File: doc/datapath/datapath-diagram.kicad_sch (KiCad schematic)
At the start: 22 parts, among them U17 ip, U19 insn, U27 stack[0], U28 stack[1], U29 ……, U32 cd_timer, U4 cstack[0], U5 cstack[1], U6 ……

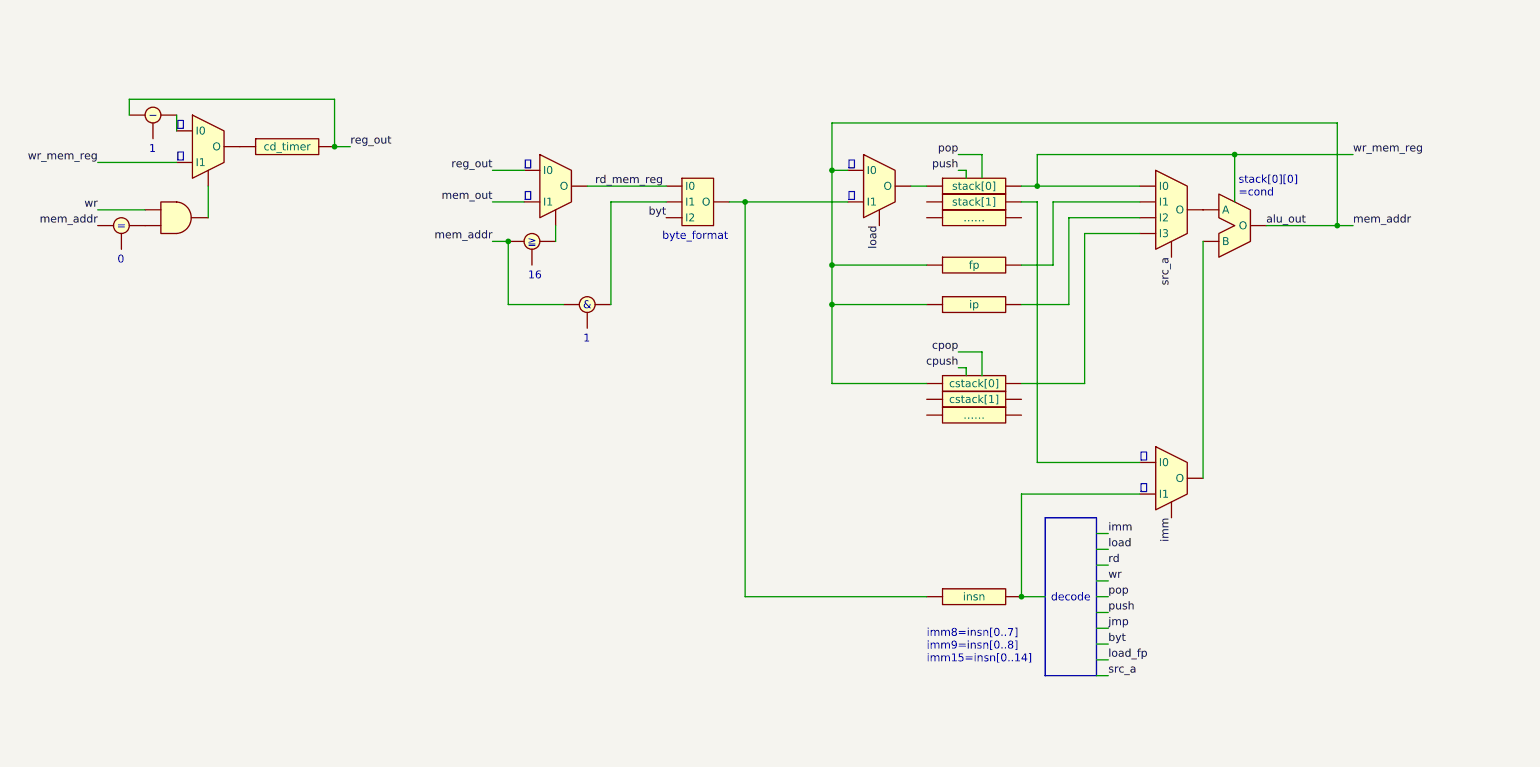
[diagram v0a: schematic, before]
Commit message: アドレスマップ（ドキュメント）を修正
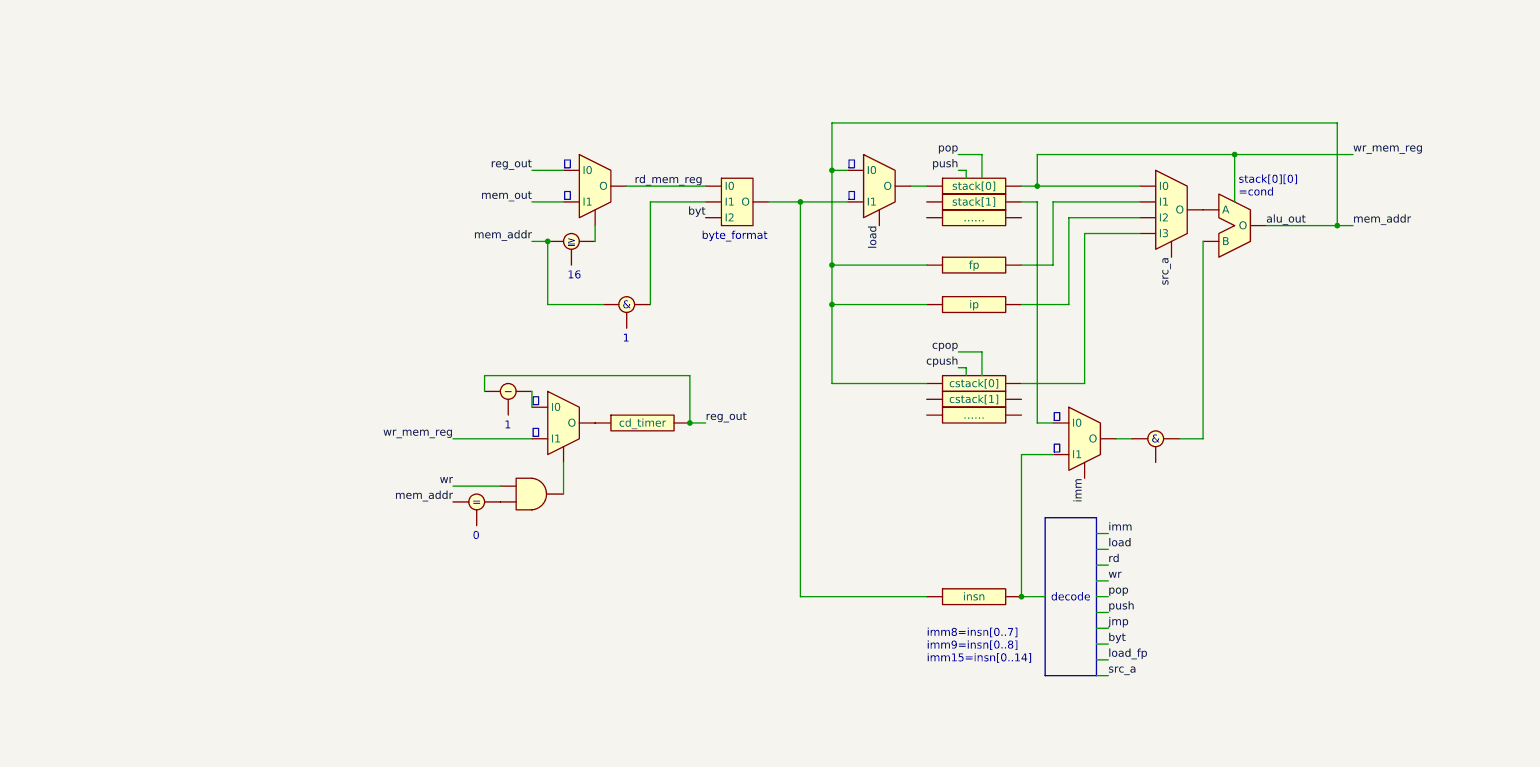
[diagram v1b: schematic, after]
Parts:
- added U2: ~, symbol Logic_Component:ALU_Circle_Left_Bottom
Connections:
- net at U28.: now also U15. (O)
- new net: U1., U31. (O)
- new net: U18. (O), U19., U34. (O)
- new net: U18. (O), U27.
- new net: U32., U36. (O)
- new net: U33., U34. (O)
- new net: U., U40. (O)
- new net: U17., U40. (O)
- new net: U4., U40. (O)
- new net: U12. (O), U40. (O)
- new net: U36. (O), U37.
- new net: U12. (O), U2.
- new net: U15. (O), U2.
- new net: U36. (O), U39.
- new net: U38., U39.

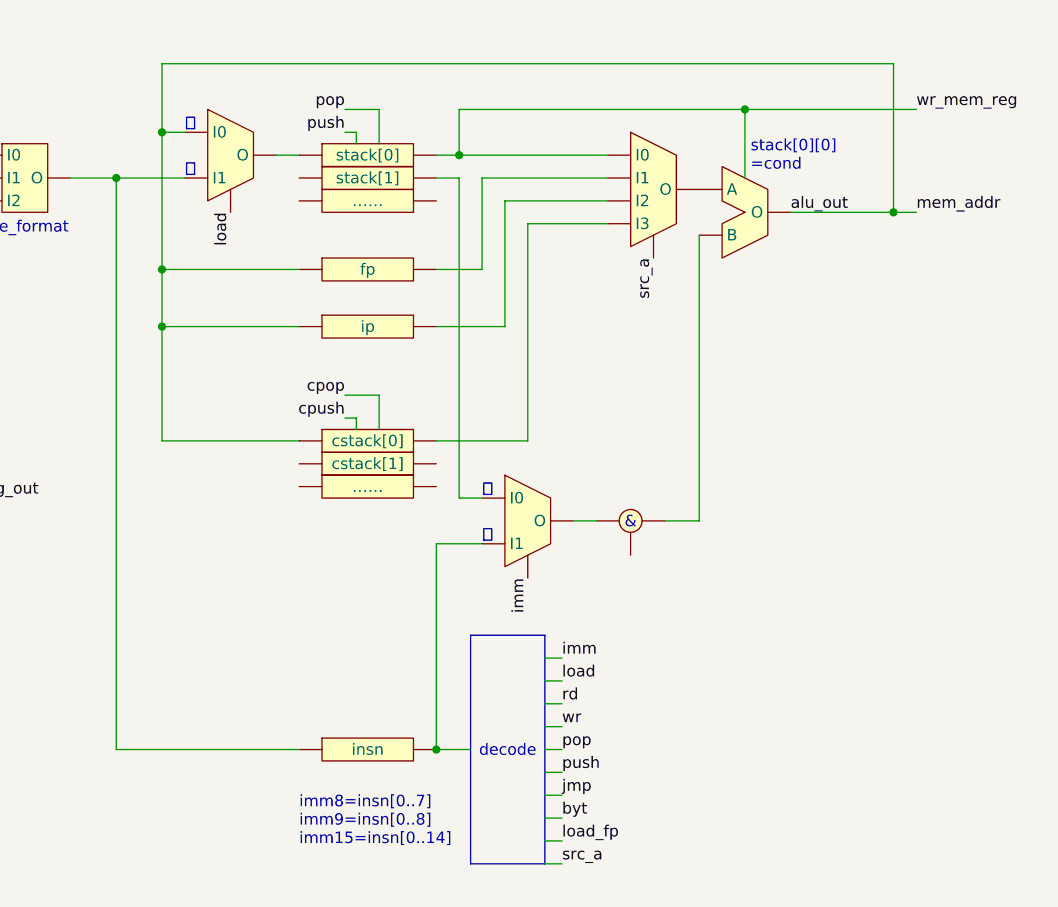
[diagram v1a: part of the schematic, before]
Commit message: データパス図を更新
メモリへ書き込むデータをstack[0]/stack[1]から選べるようにする
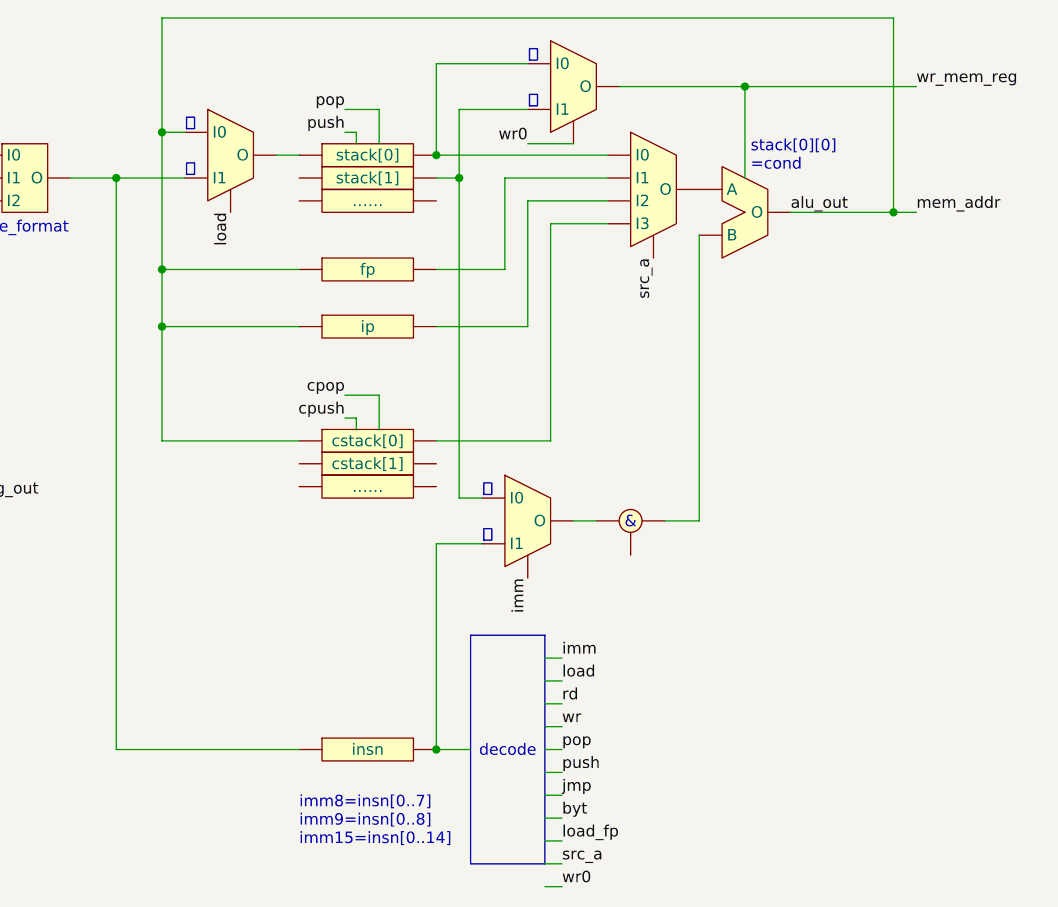
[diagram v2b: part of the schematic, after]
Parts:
- added U3: ~, symbol Logic_Component:Multiplexer_2
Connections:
- net wr_mem_reg: now also U3. (O); no longer U27., U40. (O)
- net at U28.: now also U15. (O), U3. (O)
- net at U27.: now also U40. (O), U3. (O); no longer U18. (O)
- net at U2.: now also U15. (O)
- new net: U1., U31. (O)
- new net: U18. (O), U19., U34. (O)
- new net: U18. (O), U27.
- new net: U32., U36. (O)
- new net: U33., U34. (O)
- new net: U., U40. (O)
- new net: U17., U40. (O)
- new net: U4., U40. (O)
- new net: U12. (O), U40. (O)
- new net: U36. (O), U37.
- new net: U12. (O), U2.
- new net: U36. (O), U39.
- new net: U38., U39.
- new net wr0: U3. (O)
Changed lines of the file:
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@@
   (junction (at 120.65 88.9) (diameter 0) (color 0 0 0 0)
   )
+  (junction (at 176.53 53.34) (diameter 0) (color 0 0 0 0)
+  )
+  (junction (at 173.99 50.8) (diameter 0) (color 0 0 0 0)
+  )
   (junction (at 143.51 63.5) (diameter 0) (color 0 0 0 0)
   )
@@
   (junction (at 173.99 116.84) (diameter 0) (color 0 0 0 0)
   )
+  (junction (at 208.28 43.18) (diameter 0) (color 0 0 0 0)
+  )
   (junction (at 143.51 48.26) (diameter 0) (color 0 0 0 0)
   )
-  (junction (at 208.28 45.72) (diameter 0) (color 0 0 0 0)
-  )
   (junction (at 138.43 53.34) (diameter 0) (color 0 0 0 0)
   )
-  (junction (at 176.53 50.8) (diameter 0) (color 0 0 0 0)
-  )
   (junction (at 224.79 57.15) (diameter 0) (color 0 0 0 0)
   )
+  (wire (pts (xy 186.055 132.08) (xy 187.96 132.08))
+    (stroke (width 0) (type default))
+  )
   (wire (pts (xy 167.64 77.47) (xy 167.64 81.28))
     (stroke (width 0) (type default))
@@
     (stroke (width 0) (type default))
   )
-  (wire (pts (xy 181.61 55.88) (xy 193.04 55.88))
+  (wire (pts (xy 184.15 55.88) (xy 193.04 55.88))
     (stroke (width 0) (type default))
   )
@@
     (stroke (width 0) (type default))
   )
-  (wire (pts (xy 173.99 82.55) (xy 184.15 82.55))
-    (stroke (width 0) (type default))
-  )
-  (wire (pts (xy 143.51 40.64) (xy 143.51 48.26))
+  (wire (pts (xy 173.99 82.55) (xy 186.69 82.55))
+    (stroke (width 0) (type default))
+  )
+  (wire (pts (xy 143.51 35.56) (xy 143.51 48.26))
     (stroke (width 0) (type default))
   )
@@
     (stroke (width 0) (type default))
   )
-  (wire (pts (xy 176.53 50.8) (xy 193.04 50.8))
-    (stroke (width 0) (type default))
-  )
   (wire (pts (xy 95.25 53.34) (xy 100.33 53.34))
     (stroke (width 0) (type default))
@@
     (stroke (width 0) (type default))
   )
-  (wire (pts (xy 173.99 50.8) (xy 176.53 50.8))
+  (wire (pts (xy 173.99 50.8) (xy 193.04 50.8))
     (stroke (width 0) (type default))
   )
@@
     (stroke (width 0) (type default))
   )
+  (wire (pts (xy 176.53 45.72) (xy 176.53 53.34))
+    (stroke (width 0) (type default))
+  )
   (wire (pts (xy 173.99 116.84) (xy 177.8 116.84))
     (stroke (width 0) (type default))
@@
     (stroke (width 0) (type default))
   )
+  (wire (pts (xy 184.15 49.53) (xy 189.23 49.53))
+    (stroke (width 0) (type default))
+  )
   (wire (pts (xy 186.055 121.92) (xy 187.96 121.92))
     (stroke (width 0) (type default))
@@
     (stroke (width 0) (type default))
   )
-  (wire (pts (xy 173.99 69.85) (xy 181.61 69.85))
+  (wire (pts (xy 173.99 69.85) (xy 184.15 69.85))
     (stroke (width 0) (type default))
   )
@@
     (stroke (width 0) (type default))
   )
-  (wire (pts (xy 176.53 45.72) (xy 176.53 50.8))
-    (stroke (width 0) (type default))
-  )
-  (wire (pts (xy 173.99 63.5) (xy 179.07 63.5))
+  (wire (pts (xy 173.99 40.64) (xy 173.99 50.8))
+    (stroke (width 0) (type default))
+  )
+  (wire (pts (xy 173.99 63.5) (xy 181.61 63.5))
     (stroke (width 0) (type default))
   )
@@
     (stroke (width 0) (type default))
   )
-  (wire (pts (xy 179.07 63.5) (xy 179.07 53.34))
+  (wire (pts (xy 181.61 63.5) (xy 181.61 53.34))
     (stroke (width 0) (type default))
   )
@@
     (stroke (width 0) (type default))
   )
-  (wire (pts (xy 181.61 55.88) (xy 181.61 69.85))
+  (wire (pts (xy 184.15 55.88) (xy 184.15 69.85))
     (stroke (width 0) (type default))
   )
@@
     (stroke (width 0) (type default))
   )
-  (wire (pts (xy 179.07 53.34) (xy 193.04 53.34))
-    (stroke (width 0) (type default))
-  )
-  (wire (pts (xy 224.79 40.64) (xy 224.79 57.15))
+  (wire (pts (xy 181.61 53.34) (xy 193.04 53.34))
+    (stroke (width 0) (type default))
+  )
+  (wire (pts (xy 224.79 35.56) (xy 224.79 57.15))
     (stroke (width 0) (type default))
   )
@@
     (stroke (width 0) (type default))
   )
+  (wire (pts (xy 173.99 40.64) (xy 184.15 40.64))
+    (stroke (width 0) (type default))
+  )
   (wire (pts (xy 186.055 119.38) (xy 187.96 119.38))
     (stroke (width 0) (type default))
   )
-  (wire (pts (xy 143.51 40.64) (xy 224.79 40.64))
-    (stroke (width 0) (type default))
-  )
-  (wire (pts (xy 184.15 58.42) (xy 193.04 58.42))
+  (wire (pts (xy 143.51 35.56) (xy 224.79 35.56))
+    (stroke (width 0) (type default))
+  )
+  (wire (pts (xy 186.69 58.42) (xy 193.04 58.42))
     (stroke (width 0) (type default))
   )
@@
     (stroke (width 0) (type default))
   )
-  (wire (pts (xy 208.28 45.72) (xy 208.28 53.34))
+  (wire (pts (xy 208.28 43.18) (xy 208.28 53.34))
     (stroke (width 0) (type default))
   )
@@
     (stroke (width 0) (type default))
   )
-  (wire (pts (xy 208.28 45.72) (xy 176.53 45.72))
+  (wire (pts (xy 208.28 43.18) (xy 194.31 43.18))
     (stroke (width 0) (type default))
   )
@@
     (stroke (width 0) (type default))
   )
-  (wire (pts (xy 227.33 45.72) (xy 208.28 45.72))
+  (wire (pts (xy 227.33 43.18) (xy 208.28 43.18))
     (stroke (width 0) (type default))
   )
@@
     (stroke (width 0) (type default))
   )
-  (wire (pts (xy 184.15 82.55) (xy 184.15 58.42))
+  (wire (pts (xy 186.69 82.55) (xy 186.69 58.42))
+    (stroke (width 0) (type default))
+  )
+  (wire (pts (xy 184.15 45.72) (xy 176.53 45.72))
     (stroke (width 0) (type default))
   )
@@
     (effects (font (size 1.27 1.27)))
   )
+  (text "真" (at 184.15 45.72 0)
+    (effects (font (size 1.27 1.27)) (justify left bottom))
+  )
   (text "byte_format" (at 122.555 59.69 0)
     (effects (font (size 1.27 1.27)) (justify left bottom))
@@
     (effects (font (size 1.27 1.27)) (justify left bottom))
   )
+  (text "偽" (at 184.15 40.64 0)
+    (effects (font (size 1.27 1.27)) (justify left bottom))
+  )
   (text "0" (at 85.725 107.95 0)
     (effects (font (size 1.27 1.27)) (justify left bottom))
@@
     (effects (font (size 1.27 1.27)) (justify right bottom))
   )
-  (label "wr_mem_reg" (at 227.33 45.72 0) (fields_autoplaced)
+  (label "wr_mem_reg" (at 227.33 43.18 0) (fields_autoplaced)
     (effects (font (size 1.27 1.27)) (justify left bottom))
   )
@@
   (label "mem_addr" (at 82.55 101.6 180) (fields_autoplaced)
     (effects (font (size 1.27 1.27)) (justify right bottom))
+  )
+  (label "wr0" (at 184.15 49.53 180) (fields_autoplaced)
+    (effects (font (size 1.27 1.27)) (justify right bottom))
+  )
+  (label "wr0" (at 187.96 132.08 0) (fields_autoplaced)
+    (effects (font (size 1.27 1.27)) (justify left bottom))
   )
   (label "pop" (at 187.96 116.84 0) (fields_autoplaced)
@@
         )
       )
+    )
+  )
+  (symbol (lib_id "Logic_Component:Multiplexer_2") (at 189.23 43.18 0) (unit 1)
+    (in_bom yes) (on_board yes) (dnp no)
+    (property "Reference" "U3" (at 191.77 39.37 0)
+      (effects (font (size 1.27 1.27)) hide)
+    )
+    (property "Value" "~" (at 189.23 43.18 0)
+      (effects (font (size 1.27 1.27)))
+    )
+    (property "Footprint" "" (at 189.23 43.18 0)
+      (effects (font (size 1.27 1.27)) hide)
+    )
+    (property "Datasheet" "" (at 189.23 43.18 0)
+      (effects (font (size 1.27 1.27)) hide)
+    )
+    (pin "")
+    (pin "")
+    (pin "")
+    (pin "")
+    (instances
+      (project "datapath-diagram"
+        (path "/af1fd5ae-daa0-4a17-8ab4-fe581cd231ee"
+          (reference "U3") (unit 1)
+        )
+      )
